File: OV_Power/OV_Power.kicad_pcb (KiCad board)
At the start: 2 copper layers, 174 x 57.5 mm, 85 parts, among them CN1 CONN_HEADER_R_A_2POS_2.5MM, J1 Kycon_kpjx-4s_shielded, J2 Conn_HDR_2x10_latching, J3 532530670, J4 SpadeLug, J5 SpadeLug, J6 CONN_HEADER_2.54X2_MOLEX_KK_S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, J7 CONN_HEADER_2.54X2_MOLEX_KK_S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, Q1 SSM3K341R, Q2 2N7002BK, Q3 SZNUD3124LT1G, Q4 SZNUD3124LT1G, U1 LT3796, U2 LT1936, U3 LT6106, U4 VNH5019ATR-E, U7 LTC4416, U8 AOSD21307, U9 AOSD21307

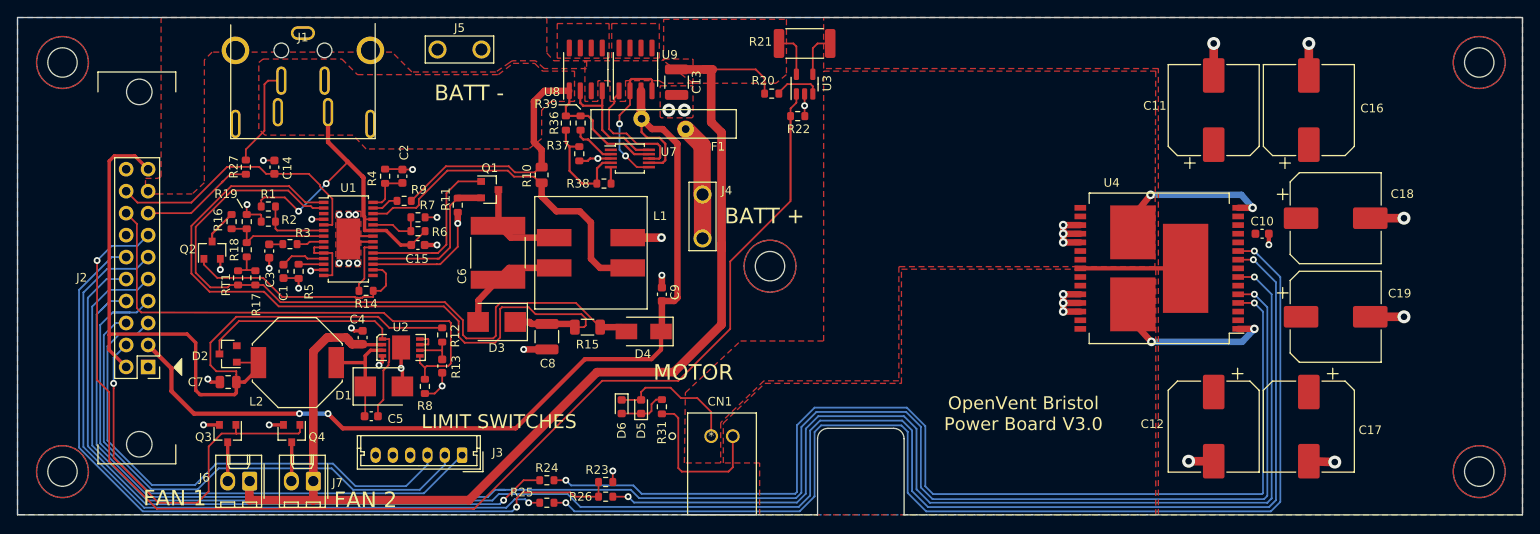
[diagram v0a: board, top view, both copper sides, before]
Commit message: Changing connectors again, also fixed a library fubar...
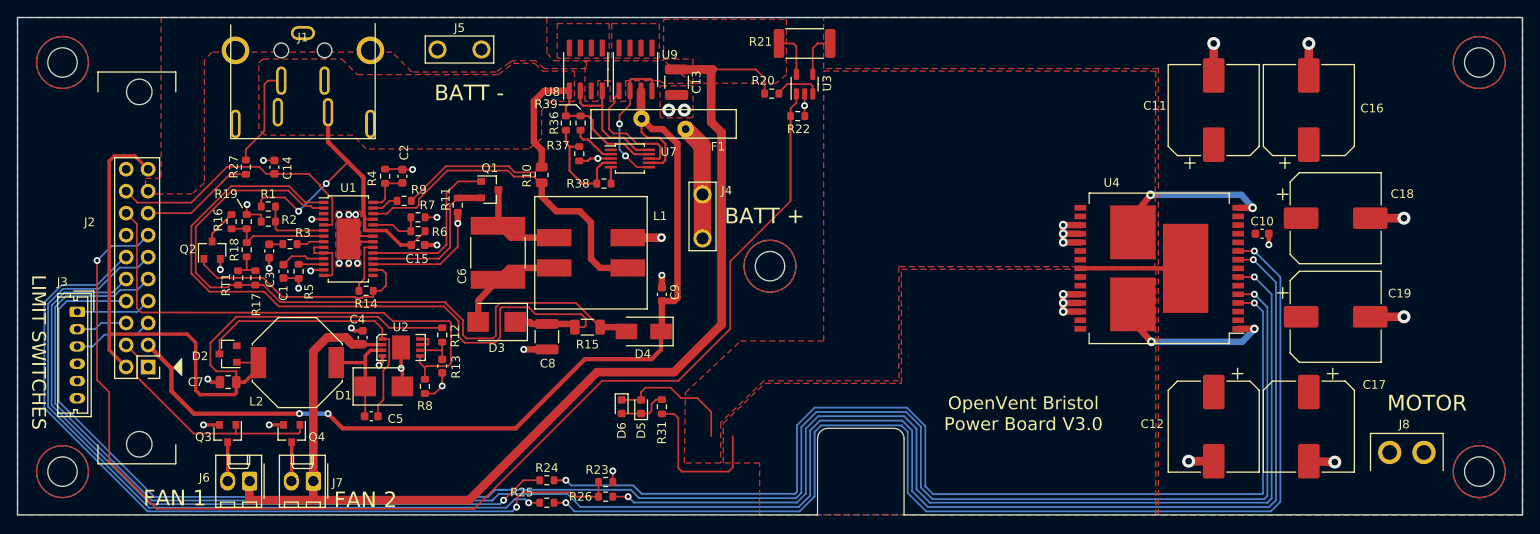
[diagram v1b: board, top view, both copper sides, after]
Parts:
- removed CN1: CONN_HEADER_R_A_2POS_2.5MM, OpenVent:53426-0210
- added J8: CONN_HEADER_R_A_2POS_JST_10A, OpenVent:JST_B2PS-VHLSN, F.Cu at (190.6, 80.3)
- moved J3 47.5 mm to (36.9, 64.0), turned to 270 degrees
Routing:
- net Net-(J2-Pad7): track 68.3 -> 8.71 mm
- net Net-(J2-Pad6): track 61.5 -> 5.95 mm
- net Net-(J2-Pad5): track 60.1 -> 9.31 mm
- net /Power Supply/FAN_DRIVE: track 45.6 -> 28.1 mm, vias 1 -> 0
- net nMOTOR-FAULT-B: track 212.0 -> 217.7 mm
- net nMOTOR-FAULT-A: track 202.6 -> 207.8 mm
- net MOTOR-IN-A: track 78.7 -> 83.7 mm
- net MOTOR-IN-B: track 83.3 -> 88.0 mm
- net PWM: track 91.8 -> 96.3 mm

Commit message: Added 3 pin JST 10amp connector for the battery.  Now all we have to worry about is connecting the wiring harness to the battery correctly...
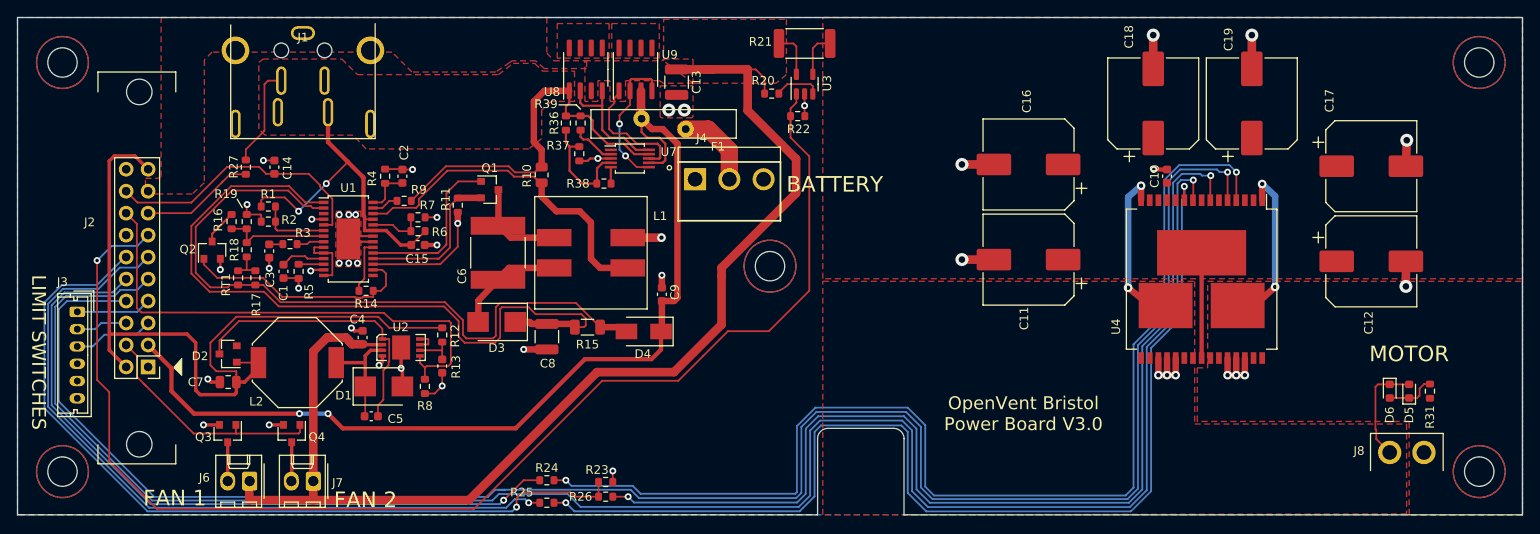
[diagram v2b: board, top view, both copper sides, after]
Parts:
- removed J5: SpadeLug, F_Connectors:TE_1217861-1
- J4: value SpadeLug -> Conn_01x03_JST_B3P_Vert; footprint F_Connectors:TE_1217861-1 -> F_Connectors:JST_B3P-VH(LF)(SN)
- moved D5 88.8 mm to (190.9, 73.2)
- moved D6 88.8 mm to (188.7, 73.2)
- moved R31 88.8 mm to (193.3, 73.2)
- moved C16 33.0 mm to (146.9, 47.0), turned to 180 degrees
- moved C17 31.0 mm to (186.5, 47.2), turned to 0 degrees
- moved C11 27.5 mm to (146.9, 58.0), turned to 180 degrees
- moved C19 26.5 mm to (172.7, 39.9), turned to 90 degrees
- moved C12 26.4 mm to (186.5, 58.2), turned to 0 degrees
- moved C18 24.9 mm to (161.3, 39.9), turned to 90 degrees
- moved C10 12.9 mm to (162.9, 48.3), turned to 90 degrees
- moved J4 5.30 mm to (112.3, 48.7), turned to 0 degrees
- moved U4 5.06 mm to (166.9, 60.2), turned to 270 degrees
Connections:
- J4 pad 1: Net-(F1-Pad1) -> GND
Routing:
- net Net-(J8-Pad2): track 37.8 -> 19.6 mm
- net Net-(R24-Pad2): track 123.8 -> 134.7 mm
- net V_MAIN: track 155.1 -> 164.1 mm
- net Net-(R25-Pad2): track 133.7 -> 125.6 mm
- net nMOTOR-FAULT-A: track 207.8 -> 215.1 mm
- net MOTOR_CURRENT: track 143.9 -> 148.5 mm
- net Net-(F1-Pad1): track 13.4 -> 9.42 mm
- net nMOTOR-FAULT-B: track 217.7 -> 213.9 mm
- net Net-(D5-Pad2): track 34.6 -> 31.5 mm
- net Net-(R26-Pad2): track 121.8 -> 123.6 mm
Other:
- board text added: "BATTERY"
- board text removed: "BATT +"
- board text removed: "BATT -"

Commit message: 12V power supply vendor changed.  Of course the pinouts for the power connector are different, argh...
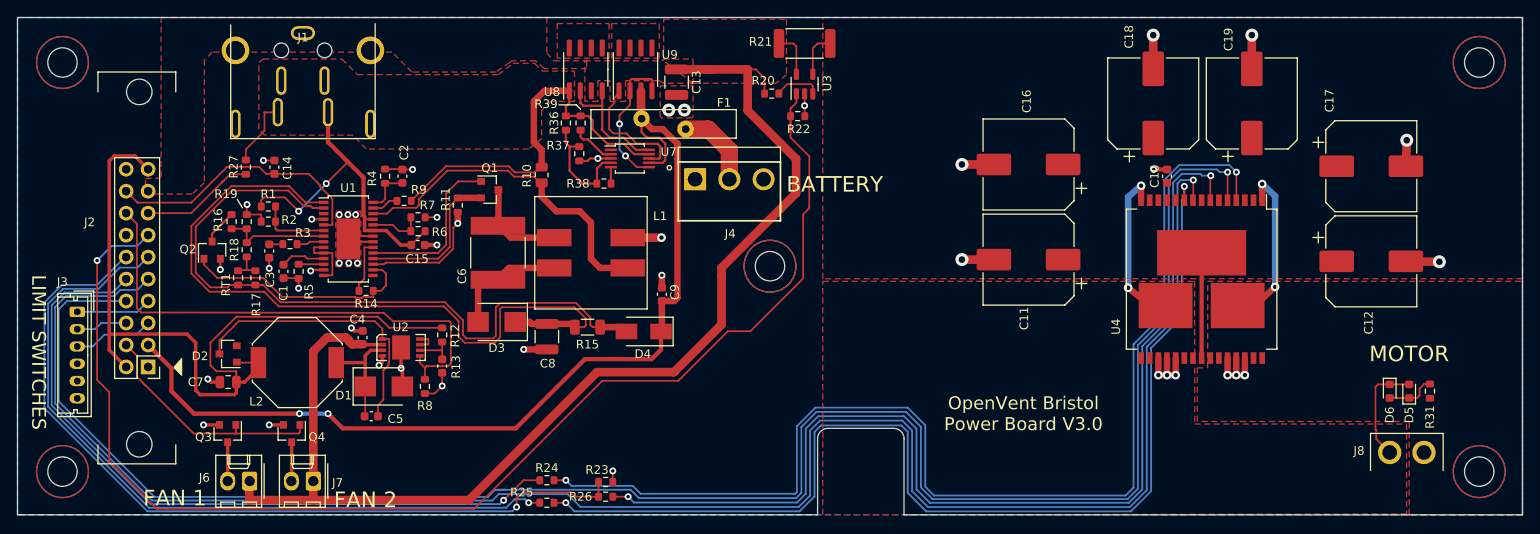
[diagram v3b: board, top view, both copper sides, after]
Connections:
- J1 pad 2: GND -> VIN_12V
- J1 pad 4: VIN_12V -> GND
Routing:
- net VIN_12V: track 95.4 -> 91.6 mm
- net Net-(C6-Pad2): track 12.8 -> 16.6 mm
- net MOTOR_CURRENT: track 148.5 -> 147.2 mm
- net /ISP_N: track 81.8 -> 82.4 mm

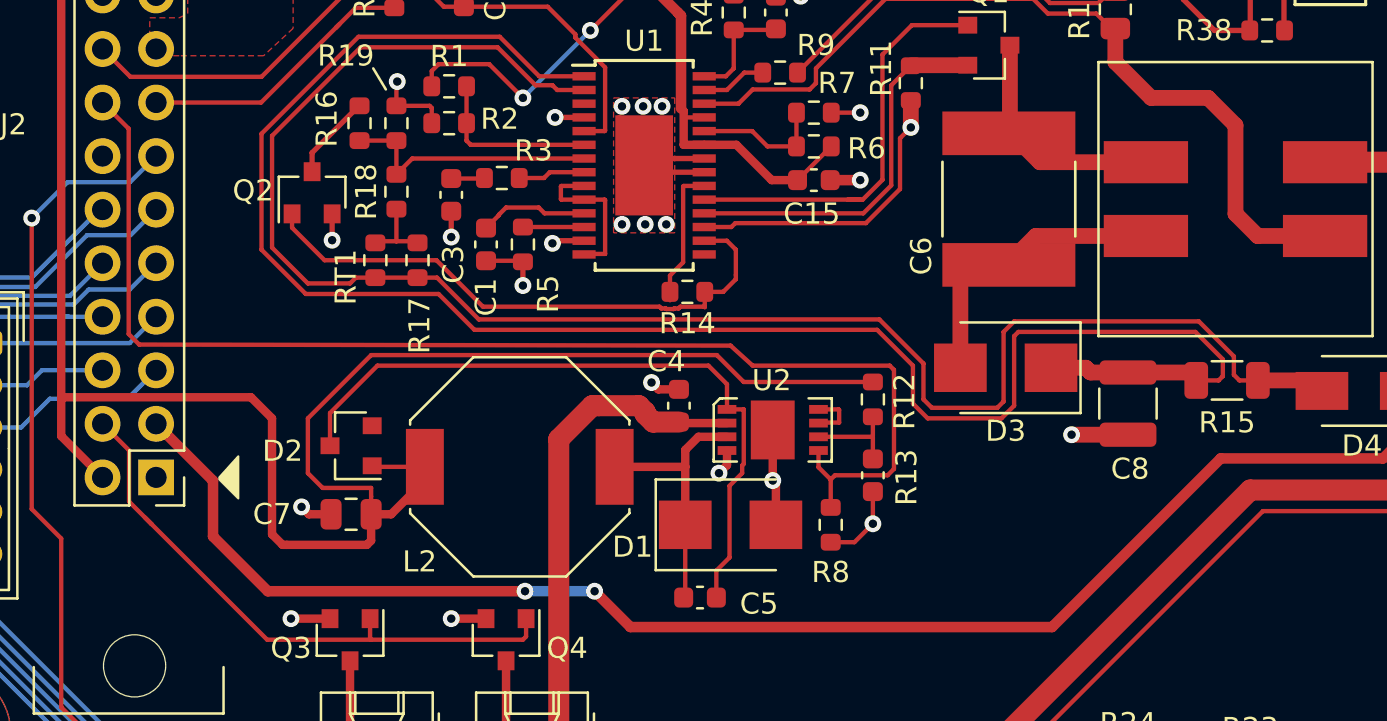
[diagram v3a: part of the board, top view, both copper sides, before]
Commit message: Minor cleanup on power supply board.  Added Sigma Delta circuitry for A/D conversion by the FPGA, just need pin assignments for all of the signals.
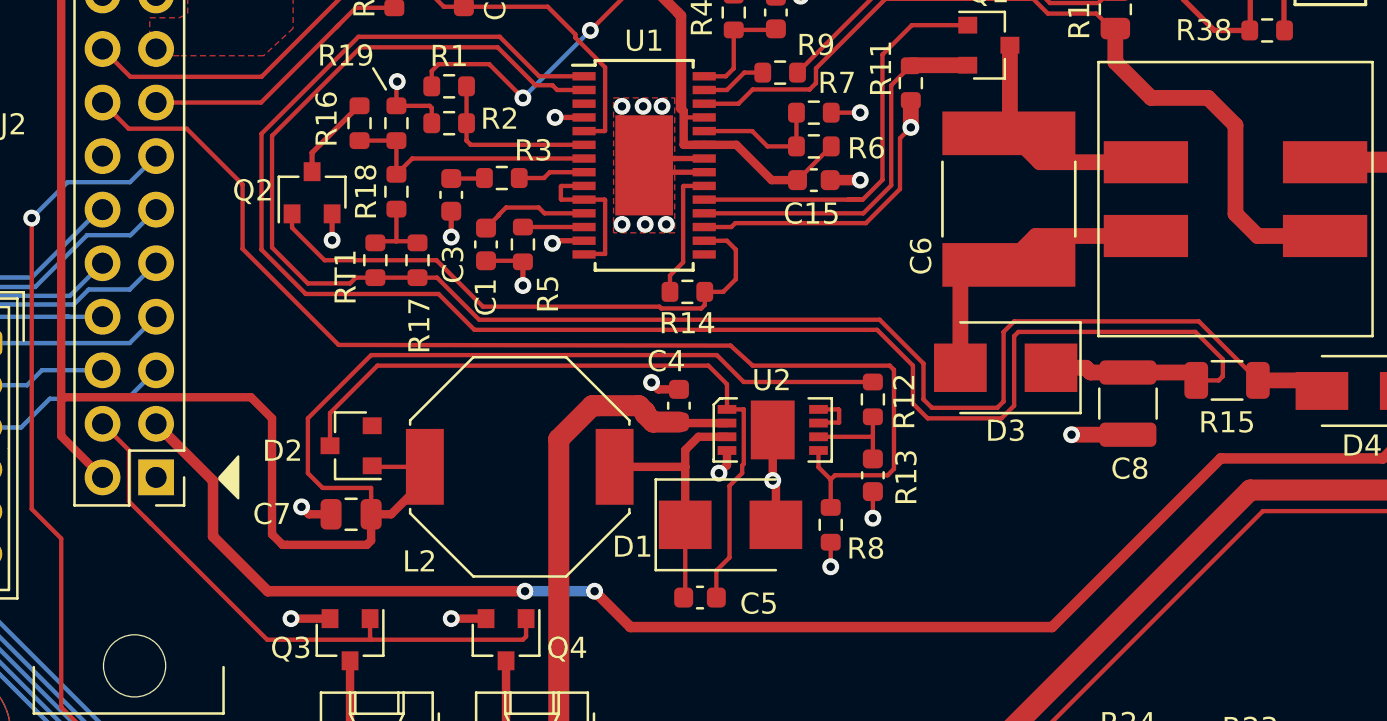
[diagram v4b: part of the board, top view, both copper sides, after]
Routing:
- net V7.5V_EN: track 59.3 -> 55.4 mm
- net GND: track 109.9 -> 108.4 mm, vias 45 -> 46
- net /ISP_N: track 82.4 -> 81.8 mm

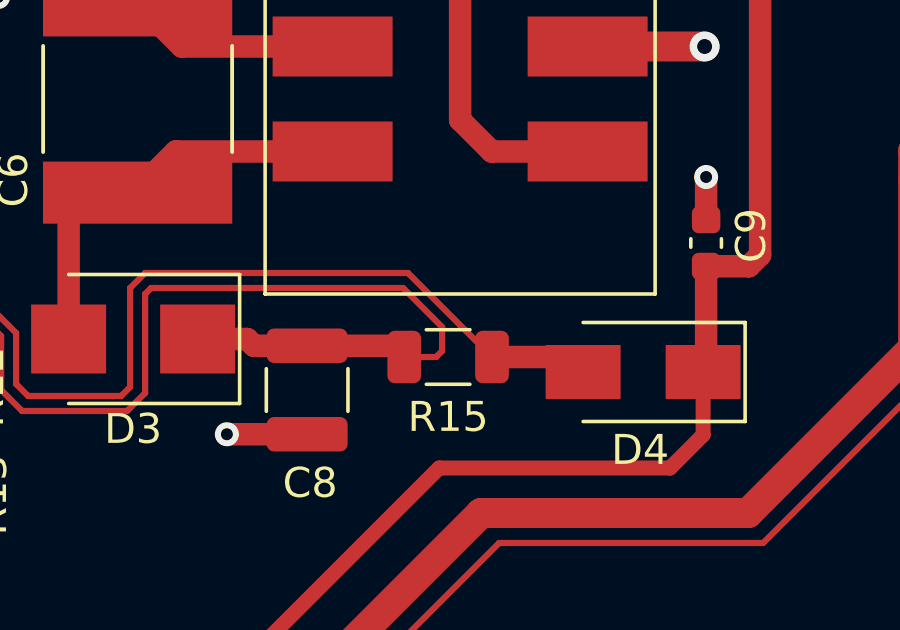
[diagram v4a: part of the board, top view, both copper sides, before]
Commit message: Sorted task OEF-412, added manufacturing output files for drill hole maps and fabrication drawing.
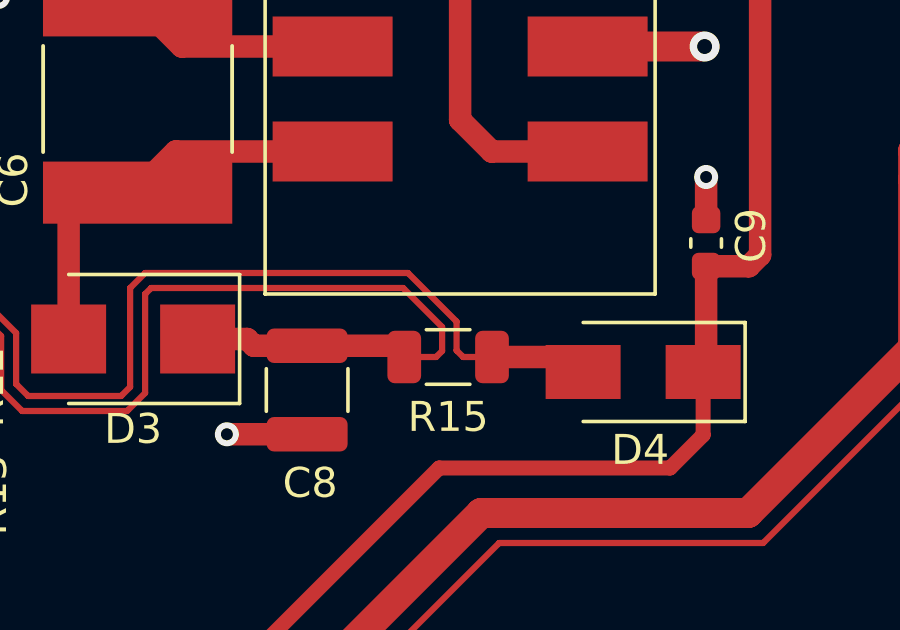
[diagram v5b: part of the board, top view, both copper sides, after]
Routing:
- net /ISP_N: track 81.8 -> 82.4 mm
